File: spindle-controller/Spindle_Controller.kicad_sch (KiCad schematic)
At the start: 25 parts, among them J1 Conn_01x19, J10 Conn_01x03, J11 Conn_01x02, J12 Conn_01x04, J13 Conn_01x02, J14 Conn_01x04, J15 GX12-6, J17 LEMO2, J18 LEMO2, J19 LEMO2, J2 Conn_01x19, J20 GX12-4, J21 GX12-2, J3 Conn_01x14, J4 Jack-DC, J5 USB_C_Receptacle_USB2.0_16P, J6 Conn_01x04, J7 Conn_01x04, J8 Conn_01x04, J9 Conn_01x05, K2 JQC-3FF-005-1Z, K3 JQC-3FF-005-1Z, K4 JQC-3FF-005-1Z, K5 JQC-3FF-005-1Z, SW1 SW_DPDT_x2

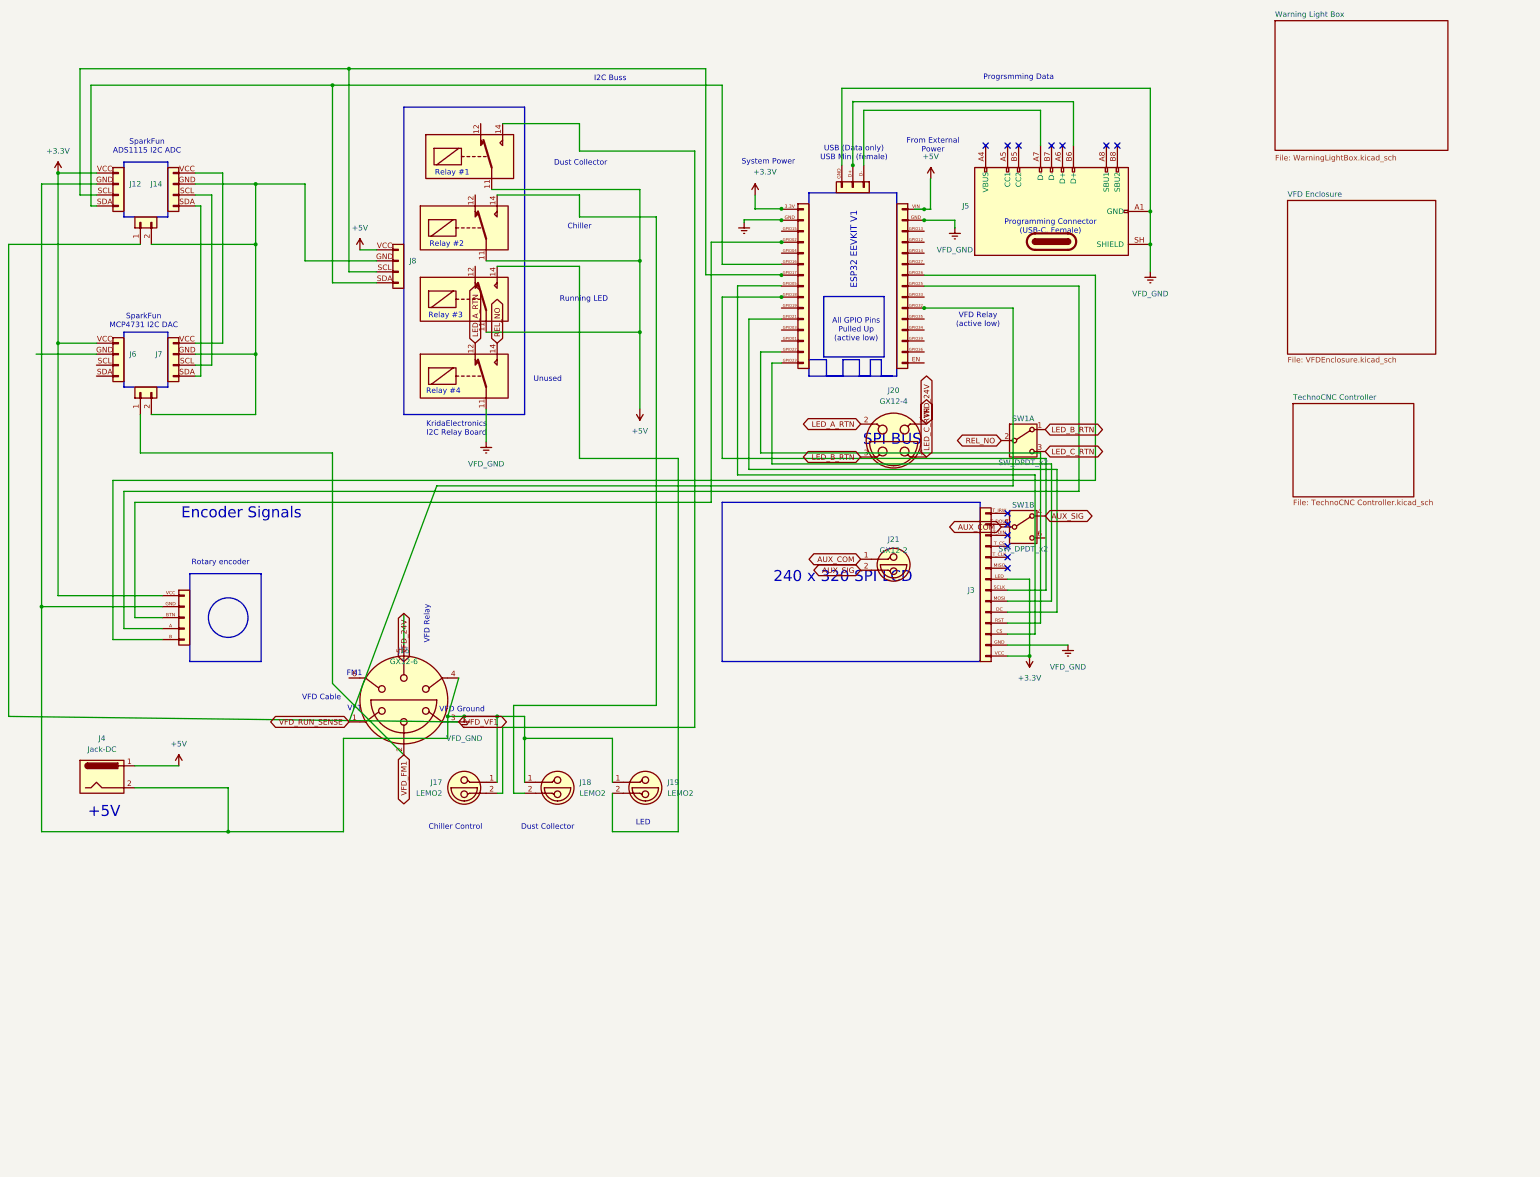
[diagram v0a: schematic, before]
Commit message: Rename project to Spindle_Controller; add VFD_DI1 spindle command path
Renamed CNC_router -> Spindle_Controller for clarity, since this
project is specifically about the spindle controller rather than the
router as a whole. Also adds the GX12-7 cable connector and VFD_DI1
wiring needed to command the spindle on, routes it through a DPDT
safety-interlock switch (SW1) shared with the warning light circuit,
fixes a DAC/ADC signal swap on VFD_VF1/VFD_FM1, and reconciles several
net labels between the root schematic and the VFD Enclosure /
TechnoCNC Controller / Warning Light Box sub-sheets.

Co-Authored-By: Claude Sonnet 5 <noreply@anthropic.com>
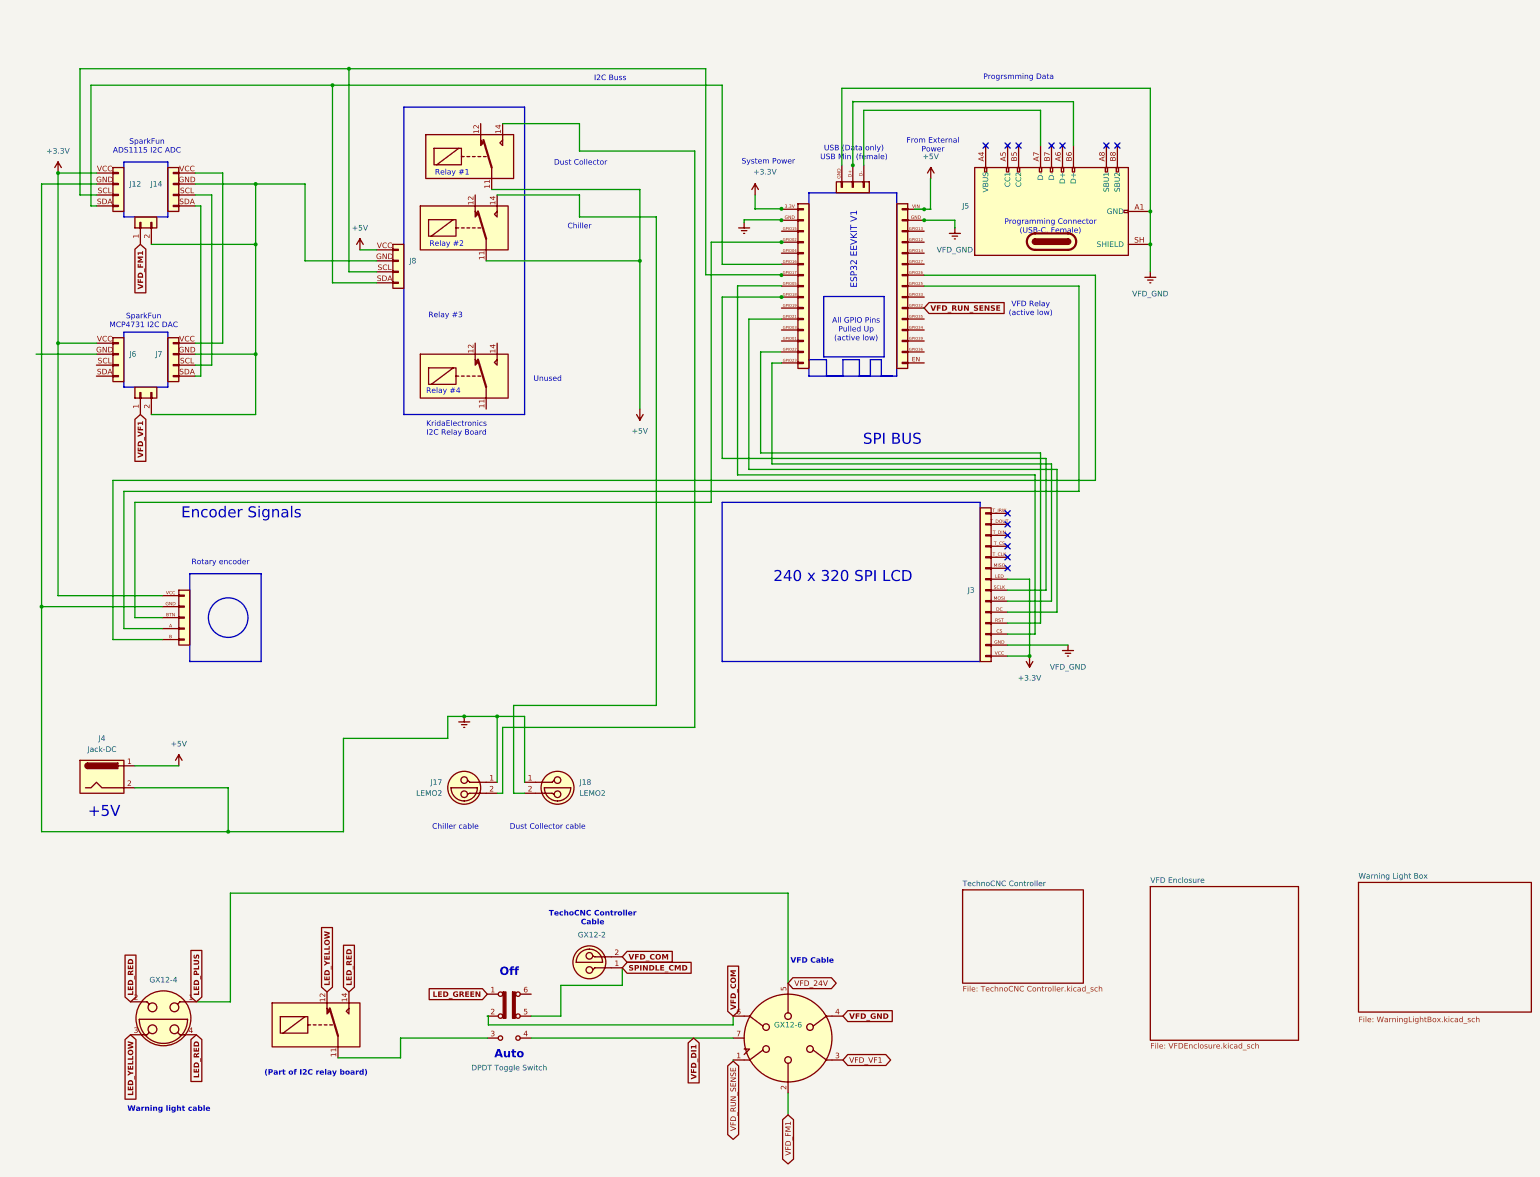
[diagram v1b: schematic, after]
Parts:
- removed J19: LEMO2, symbol Connector:LEMO2
- removed J20: GX12-4, symbol Connector:LEMO4
- removed J21: GX12-2, symbol Connector:LEMO2
- removed unit 2 of SW1
- added J19: GX12-4, symbol Connector:LEMO4
- added J26: GX12-2, symbol Connector:LEMO2
- J15: symbol Connector:LEMO6 -> GX12_Connectors:GX12-7
- SW1: value SW_DPDT_x2 -> DPDT Toggle Switch; symbol Switch:SW_DPDT_x2 -> Switch:SW_Slide_DPDT
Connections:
- net +5V: no longer K3.11
- net VFD_FM1: now also J13.1 (Pin_1); no longer J11.1 (Pin_1)
- net VFD_GND: no longer K2.11
- net VFD_VF1: now also J11.1 (Pin_1); no longer J13.1 (Pin_1)
- net LED_RED: now reaches K3.14
- net LED_RED: now also J19.2, J19.4
- net LED_YELLOW: now reaches K3.12
- net LED_YELLOW: now also J19.3
- net VFD_COM: now reaches J15.6
- net VFD_COM: now also SW1.2 (B), J26.2
- net LED_A_RTN: no longer names the net of K2.12
- net LED_B_RTN renamed LED_GREEN
- net LED_C_RTN: no longer names the net of SW1.3 (C)
- net LED_C_RTN: now also K3.11
- net REL_NO: no longer names the net of K2.14
- net REL_NO: no longer SW1.2 (B)
- new net LED_PLUS: J19.1
- new net SPINDLE_CMD: J26.1, SW1.5 (B)
- new net VFD_DI1: J15.7, SW1.4 (A)
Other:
- note added: "(Part of I2C relay board)"
- note added: "Auto"
- note added: "Chiller cable"
- note added: "Dust Collector cable"
- note added: "Off"
- note added: "TechoCNC Controller Cable"
- note added: "Warning light cable"
- note removed: "Chiller Control"
- note removed: "FM1"
- note removed: "LED"
- note removed: "Running LED"
- note removed: "VF1"
- note removed: "VFD Ground"
- note removed: "VFD Relay"
